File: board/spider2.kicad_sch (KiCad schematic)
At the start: 99 parts, among them J1 NRJ6HH-1, J10 PJ-320A, J11 PJ358, J12 PJ358, J13 PJ358, J14 PJ358, J15 PJ358, J16 PJ358, J19 PJ358, J2 NRJ6HH-1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

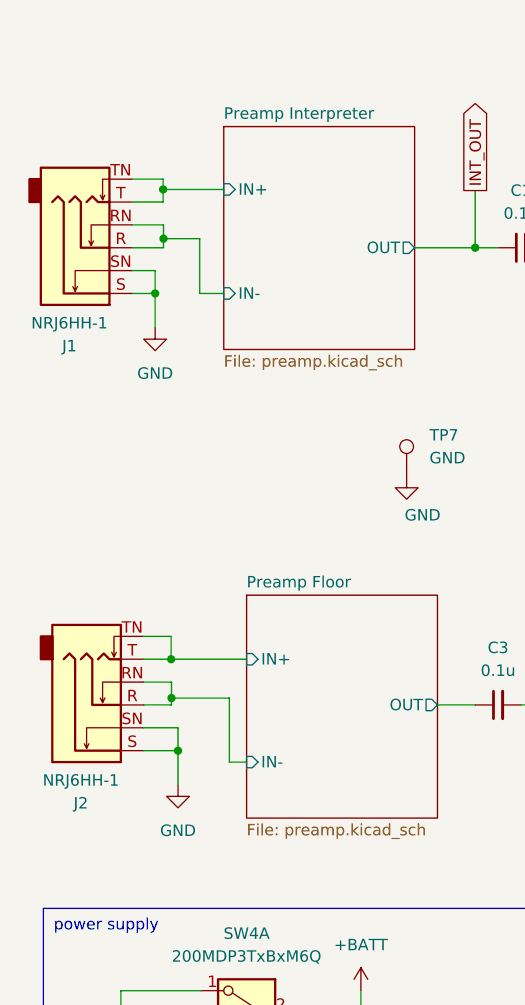
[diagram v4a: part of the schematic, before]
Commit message: 1.0: fixing wrong NRJ6HH-1 symbol
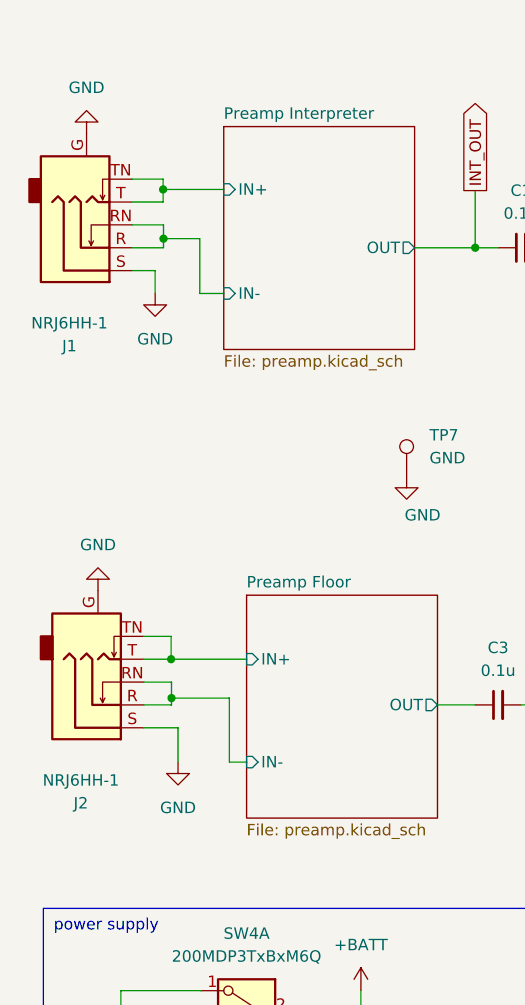
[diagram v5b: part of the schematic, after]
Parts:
- J1, J2: symbol Connector_Audio:NRJ6HH -> Connector_Audio:NRJ6HH-1
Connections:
- net GND: now also J1.G, J2.G; no longer J1.SN, J2.SN
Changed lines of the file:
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@@
 	)
 	(junction
-		(at 29.21 96.52)
-		(diameter 0)
-		(color 0 0 0 0)
-	)
-	(junction
 		(at 236.22 62.23)
 		(diameter 0)
@@
 	)
 	(junction
-		(at 26.67 45.72)
-		(diameter 0)
-		(color 0 0 0 0)
-	)
-	(junction
 		(at 158.75 107.95)
 		(diameter 0)
@@
 	(wire
 		(pts
-			(xy 26.67 45.72) (xy 26.67 49.53)
+			(xy 26.67 43.18) (xy 26.67 45.72)
 		)
 		(stroke
@@
 	(wire
 		(pts
-			(xy 29.21 96.52) (xy 25.4 96.52)
-		)
-		(stroke
-			(width 0)
-			(type default)
-		)
-	)
-	(wire
-		(pts
 			(xy 270.51 50.8) (xy 265.43 50.8)
 		)
@@
 	(wire
 		(pts
-			(xy 29.21 93.98) (xy 29.21 96.52)
+			(xy 29.21 93.98) (xy 29.21 97.79)
 		)
 		(stroke
@@
 	(wire
 		(pts
-			(xy 26.67 43.18) (xy 26.67 45.72)
-		)
-		(stroke
-			(width 0)
-			(type default)
-		)
-	)
-	(wire
-		(pts
 			(xy 243.84 111.76) (xy 247.396 111.76)
 		)
@@
 	(wire
 		(pts
-			(xy 24.13 45.72) (xy 26.67 45.72)
-		)
-		(stroke
-			(width 0)
-			(type default)
-		)
-	)
-	(wire
-		(pts
 			(xy 204.47 130.81) (xy 204.47 129.54)
 		)
@@
 	(wire
 		(pts
-			(xy 29.21 100.33) (xy 29.21 96.52)
-		)
-		(stroke
-			(width 0)
-			(type default)
-		)
-	)
-	(wire
-		(pts
 			(xy 38.1 130.81) (xy 44.45 130.81)
 		)
@@
 	(symbol
 		(lib_id "power:GND")
-		(at 26.67 49.53 0)
+		(at 26.67 45.72 0)
 		(unit 1)
 		(exclude_from_sim no)
@@
 		(fields_autoplaced yes)
 		(property "Reference" "#PWR02"
-			(at 26.67 55.88 0)
+			(at 26.67 52.07 0)
 			(effects
 				(font
@@
 		)
 		(property "Value" "GND"
-			(at 26.67 54.61 0)
+			(at 26.67 50.8 0)
 			(effects
 				(font
@@
 		)
 		(property "Footprint" ""
-			(at 26.67 49.53 0)
+			(at 26.67 45.72 0)
 			(effects
 				(font
@@
 		)
 		(property "Datasheet" ""
-			(at 26.67 49.53 0)
+			(at 26.67 45.72 0)
 			(effects
 				(font
@@
 		)
 		(property "Description" "Power symbol creates a global label with name \"GND\" , ground"
-			(at 26.67 49.53 0)
+			(at 26.67 45.72 0)
 			(effects
 				(font
@@
 	(symbol
 		(lib_id "power:GND")
-		(at 29.21 100.33 0)
+		(at 29.21 97.79 0)
 		(unit 1)
 		(exclude_from_sim no)
@@
 		(fields_autoplaced yes)
 		(property "Reference" "#PWR03"
-			(at 29.21 106.68 0)
+			(at 29.21 104.14 0)
 			(effects
 				(font
@@
 		)
 		(property "Value" "GND"
-			(at 29.21 105.41 0)
+			(at 29.21 102.87 0)
 			(effects
 				(font
@@
 		)
 		(property "Footprint" ""
-			(at 29.21 100.33 0)
+			(at 29.21 97.79 0)
 			(effects
 				(font
@@
 		)
 		(property "Datasheet" ""
-			(at 29.21 100.33 0)
+			(at 29.21 97.79 0)
 			(effects
 				(font
@@
 		)
 		(property "Description" "Power symbol creates a global label with name \"GND\" , ground"
-			(at 29.21 100.33 0)
+			(at 29.21 97.79 0)
 			(effects
 				(font
@@
 	)
 	(symbol
-		(lib_id "Connector_Audio:NRJ6HH")
+		(lib_id "Connector_Audio:NRJ6HH-1")
 		(at 20.32 91.44 0)
 		(mirror x)
@@
 			)
 		)
-		(property "Datasheet" "https://www.neutrik.com/en/product/nrj6hh"
+		(property "Datasheet" "https://www.neutrik.com/en/product/nrj6hh-1"
 			(at 20.32 91.44 0)
 			(effects
@@
 			)
 		)
-		(property "Description" "Slim Jacks, 6.35mm (1/4in) stereo jack, switched, half threaded nose"
+		(property "Description" "Slim Jacks, 6.35mm (1/4in) stereo jack, switched, half threaded nose, sleeve contact/front panel connection"
 			(at 20.32 91.44 0)
 			(effects
@@
 		(pin "S"
 		)
-		(pin "SN"
+		(pin "G"
 		)
 		(pin "R"
@@
 	)
 	(symbol
+		(lib_id "power:GND")
+		(at 19.05 27.94 180)
+		(unit 1)
+		(exclude_from_sim no)
+		(in_bom yes)
+		(on_board yes)
+		(dnp no)
+		(fields_autoplaced yes)
+		(property "Reference" "#PWR049"
+			(at 19.05 21.59 0)
+			(effects
+				(font
+					(size 1.27 1.27)
+				)
+				(hide yes)
+			)
+		)
+		(property "Value" "GND"
+			(at 19.05 22.86 0)
+			(effects
+				(font
+					(size 1.27 1.27)
+				)
+			)
+		)
+		(property "Footprint" ""
+			(at 19.05 27.94 0)
+			(effects
+				(font
+					(size 1.27 1.27)
+				)
+				(hide yes)
+			)
+		)
+		(property "Datasheet" ""
+			(at 19.05 27.94 0)
+			(effects
+				(font
+					(size 1.27 1.27)
+				)
+				(hide yes)
+			)
+		)
+		(property "Description" "Power symbol creates a global label with name \"GND\" , ground"
+			(at 19.05 27.94 0)
+			(effects
+				(font
+					(size 1.27 1.27)
+				)
+				(hide yes)
+			)
+		)
+		(pin "1"
+		)
+		(instances
+			(project "spider2"
+				(path "/31073f88-a990-4ecc-8ab9-bb6b56c98e1e"
+					(reference "#PWR049")
+					(unit 1)
+				)
+			)
+		)
+	)
+	(symbol
 		(lib_id "Device:R_Small")
 		(at 160.02 72.39 0)
@@
 	(symbol
 		(lib_id "power:GND")
+		(at 20.32 78.74 180)
+		(unit 1)
+		(exclude_from_sim no)
+		(in_bom yes)
+		(on_board yes)
+		(dnp no)
+		(fields_autoplaced yes)
+		(property "Reference" "#PWR014"
+			(at 20.32 72.39 0)
+			(effects
+				(font
+					(size 1.27 1.27)
+				)
+				(hide yes)
+			)
+		)
+		(property "Value" "GND"
+			(at 20.32 73.66 0)
+			(effects
+				(font
+					(size 1.27 1.27)
+				)
+			)
+		)
+		(property "Footprint" ""
+			(at 20.32 78.74 0)
+			(effects
+				(font
+					(size 1.27 1.27)
+				)
+				(hide yes)
+			)
+		)
+		(property "Datasheet" ""
+			(at 20.32 78.74 0)
+			(effects
+				(font
+					(size 1.27 1.27)
+				)
+				(hide yes)
+			)
+		)
+		(property "Description" "Power symbol creates a global label with name \"GND\" , ground"
+			(at 20.32 78.74 0)
+			(effects
+				(font
+					(size 1.27 1.27)
+				)
+				(hide yes)
+			)
+		)
+		(pin "1"
+		)
+		(instances
+			(project "spider2"
+				(path "/31073f88-a990-4ecc-8ab9-bb6b56c98e1e"
+					(reference "#PWR014")
+					(unit 1)
+				)
+			)
+		)
+	)
+	(symbol
+		(lib_id "power:GND")
 		(at 132.08 53.34 270)
 		(unit 1)
@@
 	)
 	(symbol
-		(lib_id "Connector_Audio:NRJ6HH")
+		(lib_id "Connector_Audio:NRJ6HH-1")
 		(at 19.05 40.64 0)
 		(mirror x)
@@
 			)
 		)
-		(property "Datasheet" "https://www.neutrik.com/media/9131/download/st-nrj6hh-1.PDF?v=2"
+		(property "Datasheet" "https://www.neutrik.com/en/product/nrj6hh-1"
 			(at 19.05 40.64 0)
 			(effects
@@
 			)
 		)
-		(property "Description" "Slim Jacks, 6.35mm (1/4in) stereo jack, switched, half threaded nose"
+		(property "Description" "Slim Jacks, 6.35mm (1/4in) stereo jack, switched, half threaded nose, sleeve contact/front panel connection"
 			(at 19.05 40.64 0)
 			(effects
@@
 		(pin "S"
 		)
-		(pin "SN"
+		(pin "G"
 		)
 		(pin "R"

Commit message: remove PJ359 footprints
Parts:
- J11, J12, J13, J14, J15, J16, J19, J20, J3, J4, J5, J7, J8, J9: footprint custom:Jack_3.5mm_Hybrid_PJ358_PJ359_20-1655 -> custom:Jack_3.5mm_Hybrid_PJ358_20-1655
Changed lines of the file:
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@@
 			)
 		)
-		(property "Footprint" "custom:Jack_3.5mm_Hybrid_PJ358_PJ359_20-1655"
+		(property "Footprint" "custom:Jack_3.5mm_Hybrid_PJ358_20-1655"
 			(at 157.48 64.77 0)
 			(effects
@@
 			)
 		)
-		(property "Footprint" "custom:Jack_3.5mm_Hybrid_PJ358_PJ359_20-1655"
+		(property "Footprint" "custom:Jack_3.5mm_Hybrid_PJ358_20-1655"
 			(at 157.48 21.59 0)
 			(effects
@@
 			)
 		)
-		(property "Footprint" "custom:Jack_3.5mm_Hybrid_PJ358_PJ359_20-1655"
+		(property "Footprint" "custom:Jack_3.5mm_Hybrid_PJ358_20-1655"
 			(at 209.55 21.59 0)
 			(effects
@@
 			)
 		)
-		(property "Footprint" "custom:Jack_3.5mm_Hybrid_PJ358_PJ359_20-1655"
+		(property "Footprint" "custom:Jack_3.5mm_Hybrid_PJ358_20-1655"
 			(at 191.77 64.77 0)
 			(effects
@@
 			)
 		)
-		(property "Footprint" "custom:Jack_3.5mm_Hybrid_PJ358_PJ359_20-1655"
+		(property "Footprint" "custom:Jack_3.5mm_Hybrid_PJ358_20-1655"
 			(at 156.21 90.17 0)
 			(effects
@@
 			)
 		)
-		(property "Footprint" "custom:Jack_3.5mm_Hybrid_PJ358_PJ359_20-1655"
+		(property "Footprint" "custom:Jack_3.5mm_Hybrid_PJ358_20-1655"
 			(at 191.77 43.18 0)
 			(effects
@@
 			)
 		)
-		(property "Footprint" "custom:Jack_3.5mm_Hybrid_PJ358_PJ359_20-1655"
+		(property "Footprint" "custom:Jack_3.5mm_Hybrid_PJ358_20-1655"
 			(at 173.99 21.59 0)
 			(effects
@@
 			)
 		)
-		(property "Footprint" "custom:Jack_3.5mm_Hybrid_PJ358_PJ359_20-1655"
+		(property "Footprint" "custom:Jack_3.5mm_Hybrid_PJ358_20-1655"
 			(at 209.55 64.77 0)
 			(effects
@@
 			)
 		)
-		(property "Footprint" "custom:Jack_3.5mm_Hybrid_PJ358_PJ359_20-1655"
+		(property "Footprint" "custom:Jack_3.5mm_Hybrid_PJ358_20-1655"
 			(at 173.99 90.17 0)
 			(effects
@@
 			)
 		)
-		(property "Footprint" "custom:Jack_3.5mm_Hybrid_PJ358_PJ359_20-1655"
+		(property "Footprint" "custom:Jack_3.5mm_Hybrid_PJ358_20-1655"
 			(at 209.55 43.18 0)
 			(effects
@@
 			)
 		)
-		(property "Footprint" "custom:Jack_3.5mm_Hybrid_PJ358_PJ359_20-1655"
+		(property "Footprint" "custom:Jack_3.5mm_Hybrid_PJ358_20-1655"
 			(at 173.99 43.18 0)
 			(effects
@@
 			)
 		)
-		(property "Footprint" "custom:Jack_3.5mm_Hybrid_PJ358_PJ359_20-1655"
+		(property "Footprint" "custom:Jack_3.5mm_Hybrid_PJ358_20-1655"
 			(at 191.77 21.59 0)
 			(effects
@@
 			)
 		)
-		(property "Footprint" "custom:Jack_3.5mm_Hybrid_PJ358_PJ359_20-1655"
+		(property "Footprint" "custom:Jack_3.5mm_Hybrid_PJ358_20-1655"
 			(at 157.48 43.18 0)
 			(effects
@@
 			)
 		)
-		(property "Footprint" "custom:Jack_3.5mm_Hybrid_PJ358_PJ359_20-1655"
+		(property "Footprint" "custom:Jack_3.5mm_Hybrid_PJ358_20-1655"
 			(at 173.99 64.77 0)
 			(effects

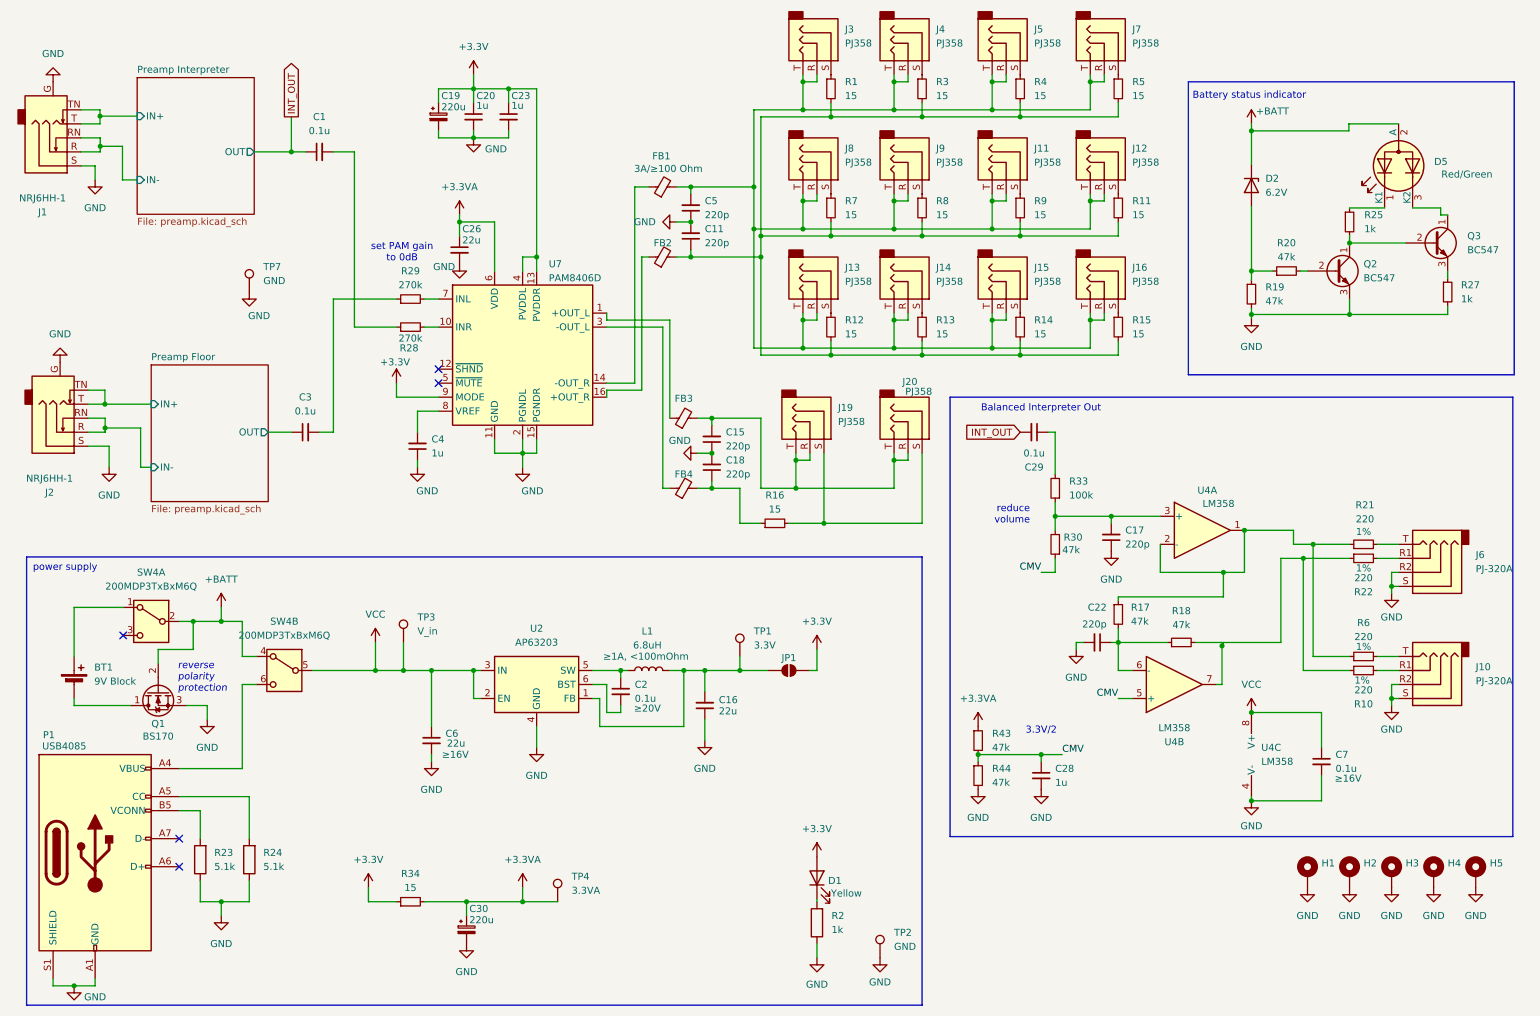
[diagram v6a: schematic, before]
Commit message: version 1.1
- replace MAX4062 with own preamplifier circuit in order to avoid difficult TSOP soldering
- easier solderable USB-C port
- add linear regulator for stable 1.65V
- replace LM358 with rail-to-rail and 3.3V compatible OPA2310 op amp
- rounded corners
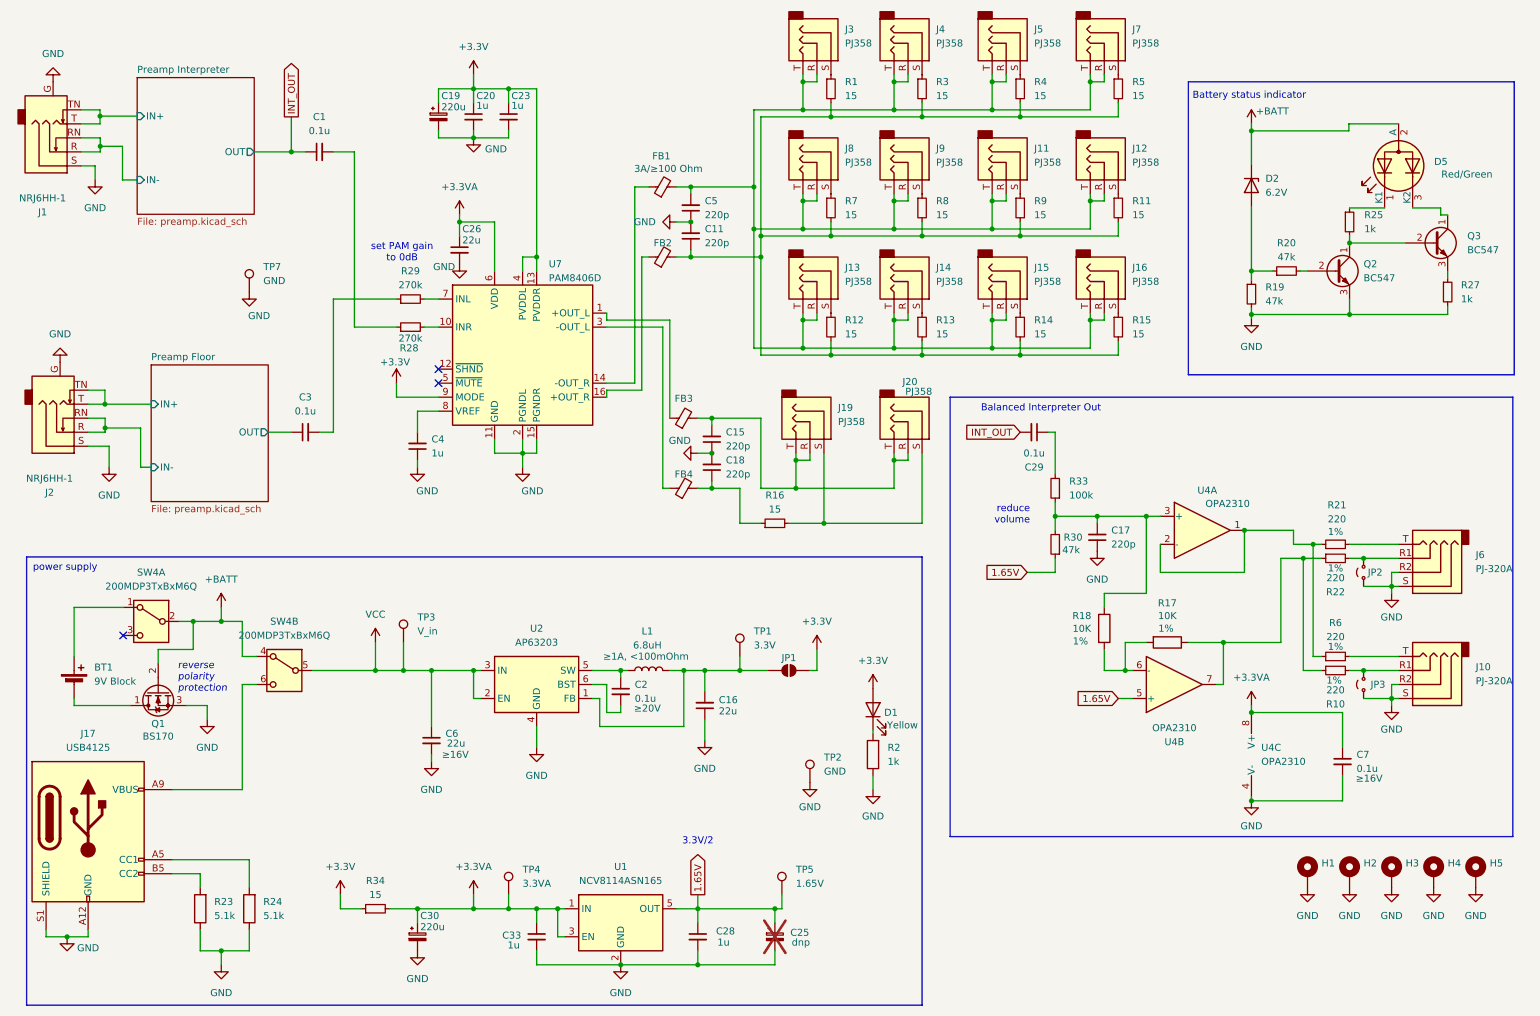
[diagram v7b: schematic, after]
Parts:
- removed C22: 220p, Capacitor_THT:C_Disc_D3.0mm_W2.0mm_P2.50mm, symbol Device:C_Small
- removed P1: USB4085, Connector_USB:USB_C_Receptacle_GCT_USB4085, symbol Connector:USB_C_Plug_USB2.0
- removed R17, R18, R43, R44: 47k, Resistor_THT:R_Axial_DIN0207_L6.3mm_D2.5mm_P10.16mm_Horizontal, symbol Device:R_Small
- added C25: dnp, Capacitor_THT:CP_Radial_D6.3mm_P2.50mm, symbol Device:C_Polarized_Small
- added C33: 1u, Capacitor_THT:C_Disc_D4.3mm_W1.9mm_P5.00mm, symbol Device:C_Small
- added J17: USB4125, Connector_USB:USB_C_Receptacle_GCT_USB4125-xx-x_6P_TopMnt_Horizontal, symbol Connector:USB_C_Receptacle_PowerOnly_6P
- added JP2, JP3: ~, Jumper:SolderJumper-2_P1.3mm_Open_RoundedPad1.0x1.5mm, symbol Jumper:Jumper_2_Small_Open
- added R17, R18: 10K, Resistor_THT:R_Axial_DIN0204_L3.6mm_D1.6mm_P5.08mm_Horizontal, symbol Device:R
- added TP5: 1.65V, TestPoint:TestPoint_THTPad_1.5x1.5mm_Drill0.7mm, symbol Connector:TestPoint
- added U1: NCV8114ASN165, Package_TO_SOT_SMD:TSOT-23-5, symbol Regulator_Linear:NCV8114ASN165T1G
- U4: value LM358 -> OPA2310; footprint Package_DIP:DIP-8_W7.62mm -> Package_SO:SOIC-8_3.9x4.9mm_P1.27mm
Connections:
- net +3.3VA: now also C7.1, U4.8 (V+), C33.1, U1.1 (IN), U1.3 (EN)
- net GND: now also C25.2, C33.2, J17.A12 (GND), J17.B12 (GND), J17.S1 (SHIELD), JP2.1 (A), JP3.1 (A), U1.2 (GND)
- net VCC: no longer C7.1, U4.8 (V+)
- net at U4.6 (-): now also R17.2, R18.2
- net at R10.1, R22.1, U4.7: now also R17.1
- net at J6.R1, R22.2: now also JP2.2 (B)
- net at C17.2, R30.2, R33.1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: now also R18.1
- net at J10.R1, R10.2: now also JP3.2 (B)
- net at R23.2: now also J17.B5 (CC2)
- net at R24.2: now also J17.A5 (CC1)
- net at SW4.6 (C): now also J17.A9 (VBUS), J17.B9 (VBUS)
- net CMV renamed 1.65V
- net 1.65V: now also C25.1, TP5.1, U1.5 (OUT)
- no-connect marks 5 -> 3
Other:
- moved on the sheet: C17, C30, C7, D1, R10, R2, R21, R22, R23, R24, R34, R6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
